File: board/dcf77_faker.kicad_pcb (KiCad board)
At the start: 4 copper layers, 69 x 32 mm, 49 parts, among them J1 Barrel_Jack, J2 DBG, J3 ANT, J4 LCD_I2C, SW1 RST, SW2 H, SW3 MIN, SW4 S, U1 NCP1117ST33T3G, U2 ATSAML21G18B-AUT, X1 32.768kHz, X2 31MHz

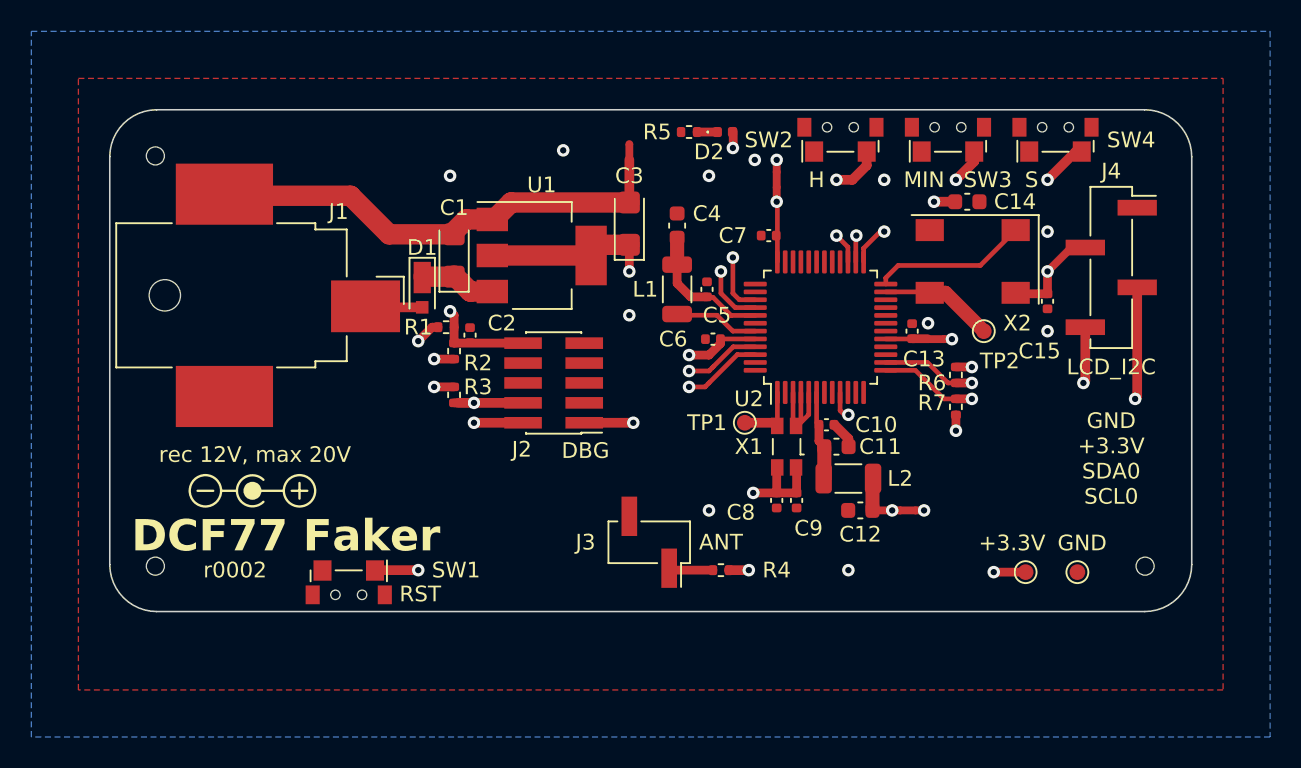
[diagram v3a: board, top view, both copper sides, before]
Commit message: board: hierarchical sheets, renumber components
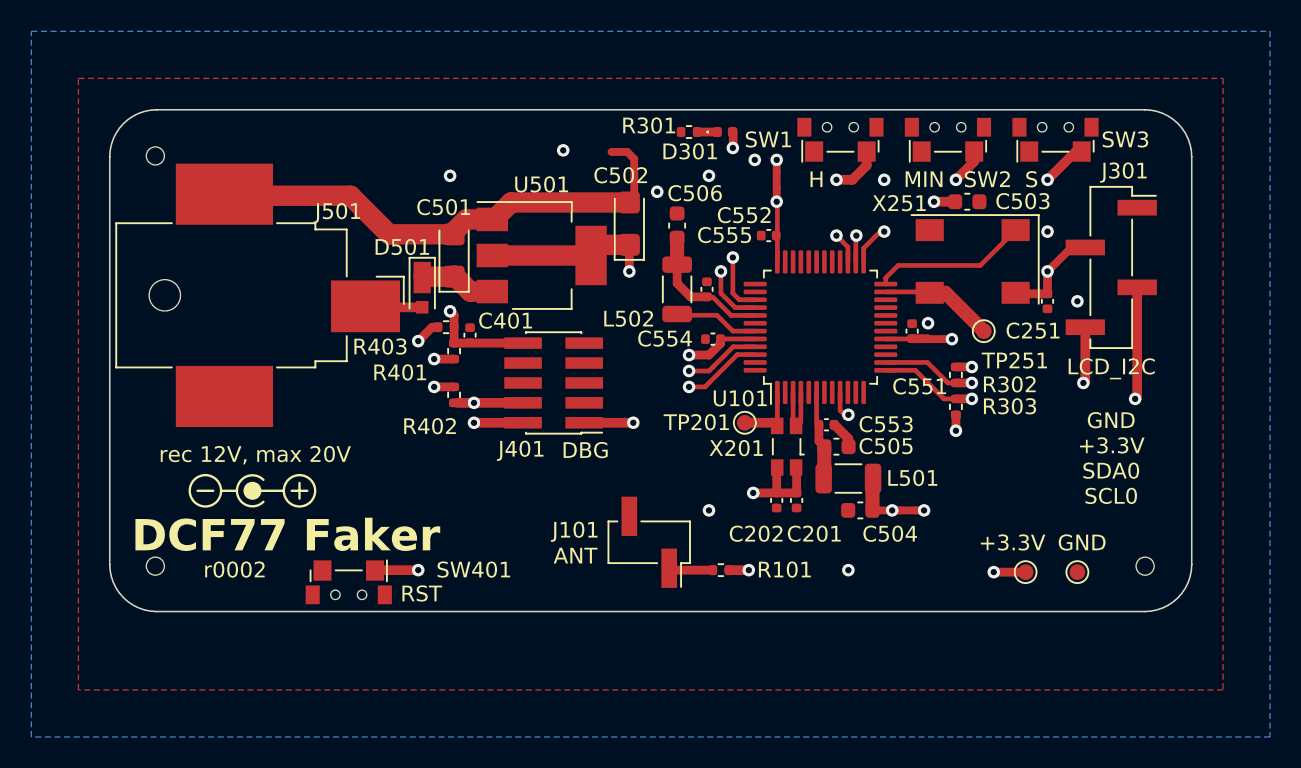
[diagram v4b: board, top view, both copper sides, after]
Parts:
- moved NT501 0.63 mm to (182.5, 59.7), turned to 180 degrees
- renumbered C9 to C201, C8 to C202, C15 to C251, C2 to C401, C1 to C501, C3 to C502, C14 to C503, C12 to C504, C11 to C505, C4 to C506, C13 to C551, C7 to C552, C10 to C553, C6 to C554, C5 to C555, D2 to D301, D1 to D501, J3 to J101, J4 to J301, J2 to J401, J1 to J501, L2 to L501, L1 to L502, NT1 to NT501, NT2 to NT502, NT4 to NT503, NT3 to NT504, R4 to R101, R5 to R301, R6 to R302, R7 to R303, R2 to R401, R3 to R402, R1 to R403, SW2 to SW1, SW3 to SW2, SW4 to SW3, SW1 to SW401, TP1 to TP201, TP2 to TP251, TP3 to TP501, TP4 to TP502, U2 to U101, U1 to U501, X1 to X201, X2 to X251
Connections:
- net +3.3V renamed /+3.3V
- net /RAWGND renamed /power supply/RAWGND
- net /SWCLK renamed /debug & reset/SWCLK
- net /SWDIO renamed /debug & reset/SWDIO
- net /~{RST} renamed /debug & reset/~{RST}
- C201 pad 1: GND -> /GND
- C202 pad 1: GND -> /GND
- C251 pad 1: GND -> /GND
- C401 pad 1: GND -> /GND
- C503 pad 2: GND -> /GND
- C504 pad 2: GND -> /GND
- C505 pad 2: GND -> /GND
- C506 pad 2: GND -> /GND
- C551 pad 2: GND -> /GND
- C552 pad 2: GND -> /GND
- C553 pad 2: GND -> /GND
- C554 pad 2: GND -> /GND
- C555 pad 2: GND -> /GND
- J101 pad 2: GND -> /GND
- J301 pad 1: GND -> /GND
- J401 pad 3: GND -> /GND
- J401 pad 5: GND -> /GND
- NT501 pad 2: GND -> /GND
- R301 pad 1: GND -> /GND
- SW1 pad 1: GND -> /GND
- SW2 pad 1: GND -> /GND
- SW3 pad 1: GND -> /GND
- SW401 pad 2: GND -> /GND
- TP502 pad 1: GND -> /GND
- U101 pad 18: GND -> /GND
- U101 pad 3: GND -> /GND
- U101 pad 35: GND -> /GND
- U101 pad 4: GND -> /GND
- U101 pad 42: GND -> /GND
- U101 pad 47: GND -> /GND
- U101 pad 48: GND -> /GND
- U101 pad 5: GND -> /GNDANA
- X201 pad 2: GND -> /GND
- X251 pad 2: GND -> /GND
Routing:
- net GND: track 7.79 -> 0.00 mm, vias 5 -> 0
- net /GND: track 0.00 -> 5.67 mm, vias 0 -> 5
- net /power supply/RAWGND: track 30.1 -> 30.9 mm
- added copper zone on B.Cu, net /GND
- added copper zone on F.Cu, net /GND
- removed copper zone on B.Cu, net GND
- removed copper zone on F.Cu, net GND
